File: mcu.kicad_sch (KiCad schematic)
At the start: 5 parts, among them J3 USB_C_Receptacle_USB2.0_16P, M1 Module-stlink-0.1, M3 Module-mega-mcu144-0.6

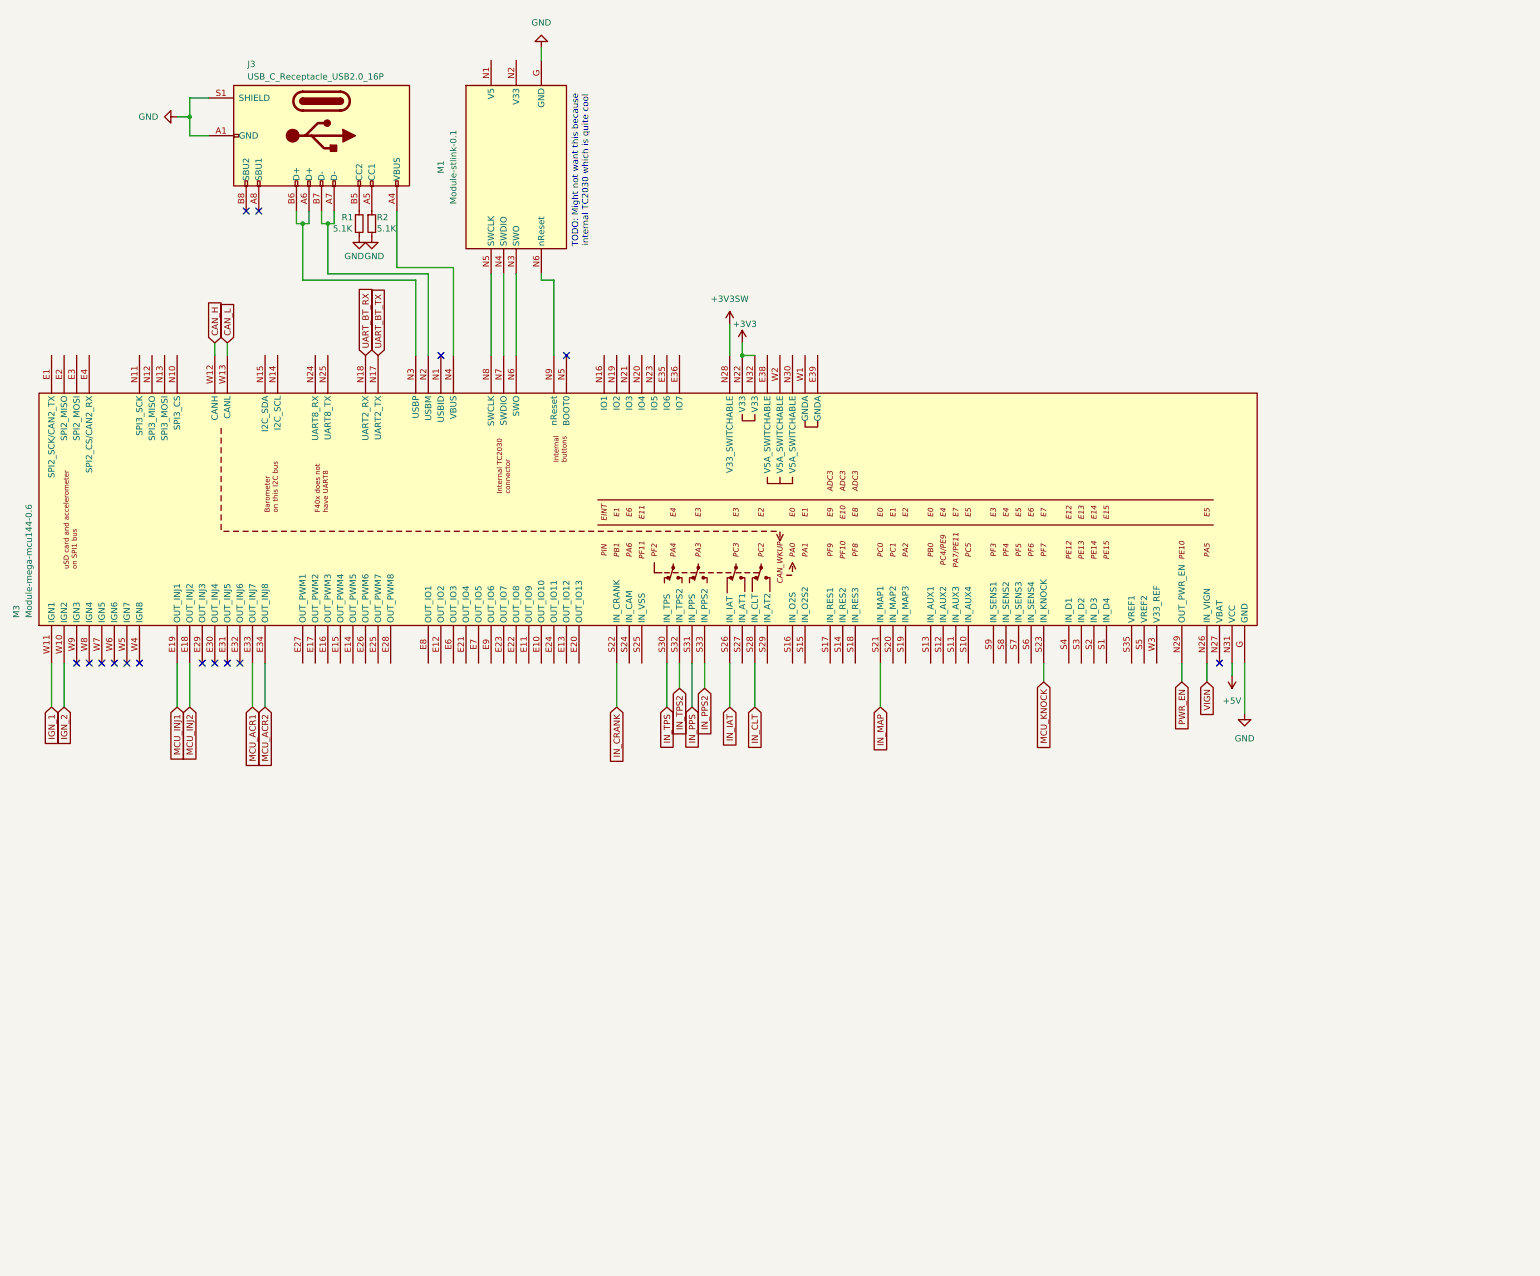
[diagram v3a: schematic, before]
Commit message: igntion igbt, cooling mosfet
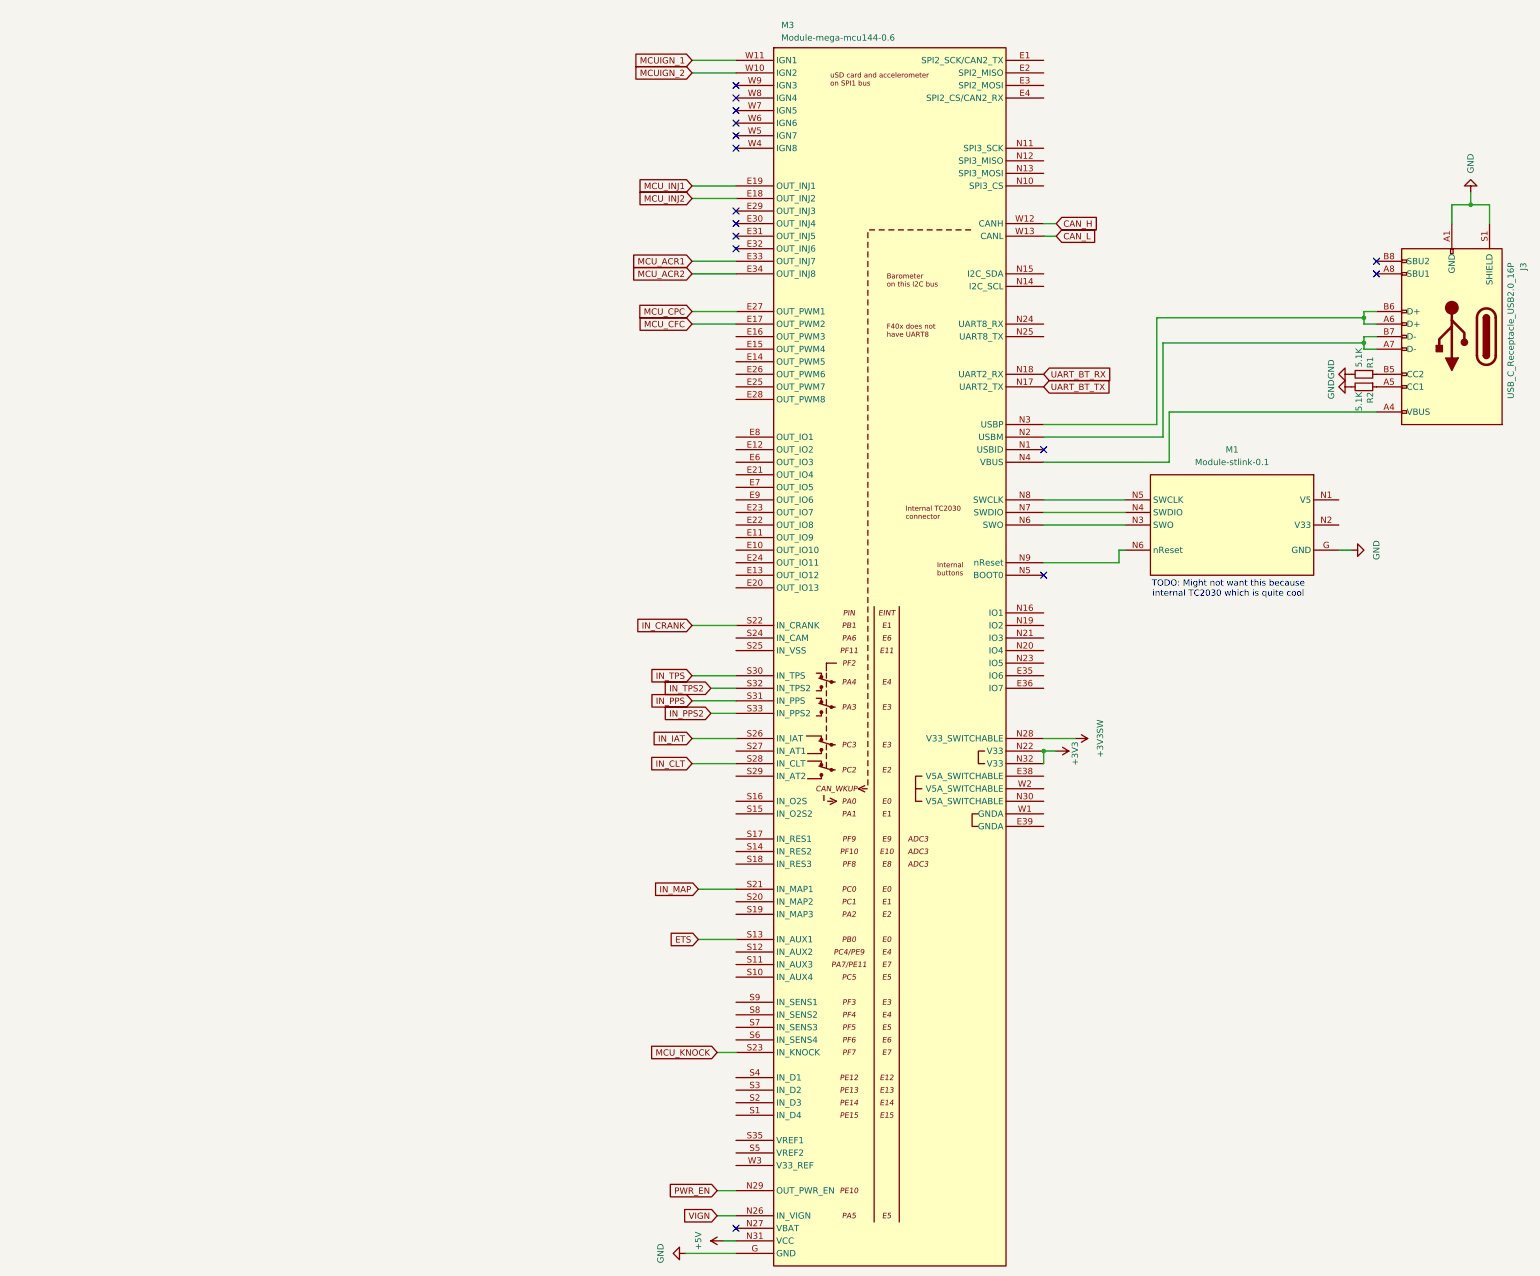
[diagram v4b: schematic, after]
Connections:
- net MCU_CFC: now reaches M3.E17 (OUT_PWM2)
- net MCU_CPC: now reaches M3.E27 (OUT_PWM1)
- net ETS: now reaches M3.S13 (IN_AUX1)
- net IGN_1 renamed MCUIGN_1
- net IGN_2 renamed MCUIGN_2
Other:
- moved on the sheet: J3, M1, M3, R1, R2

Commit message: trying out a layout and routing
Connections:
- net +5VA: now reaches M3.E38 (V5A_SWITCHABLE)
- net +5VA: now also M3.W2 (V5A_SWITCHABLE)
- net H2OSPC: now reaches M3.S11 (IN_AUX3)
- net H2OS2: now reaches M3.S15 (IN_O2S2)
- net H2OS1: now reaches M3.S16 (IN_O2S)
- net IN_JSS: now reaches M3.S17 (IN_RES1)
- net IN_AAT: now reaches M3.S27 (IN_AT1)
- net MCU_KNOCK_R: now reaches M3.S9 (IN_SENS1)
- net GNDA: now reaches M3.W1 (GNDA)
- net MCU_KNOCK renamed MCU_KNOCK_F
- no-connect marks 15 -> 17
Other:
- note added: "TODO: Do we really need post CAT?"

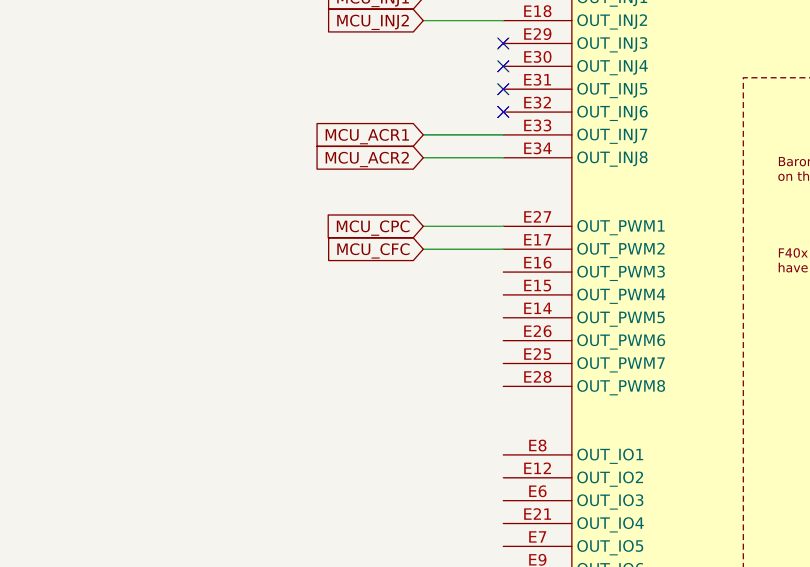
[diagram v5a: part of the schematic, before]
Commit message: adding electronic throttle control
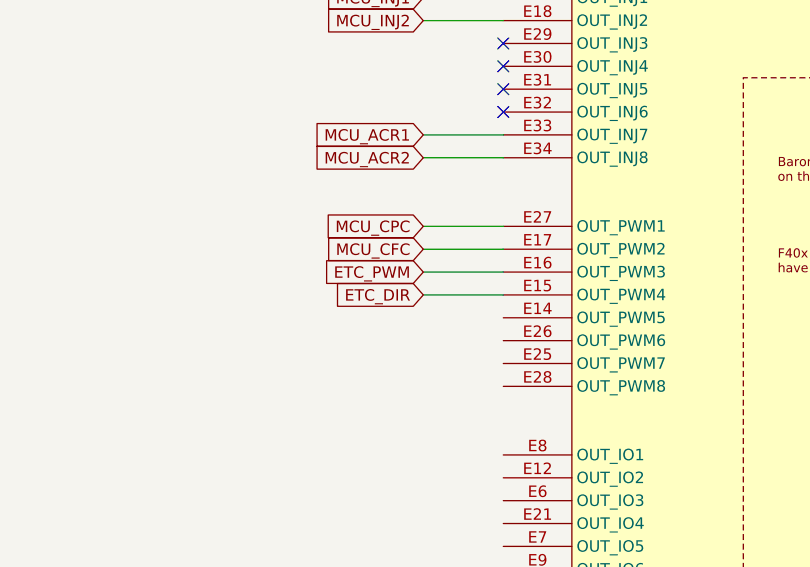
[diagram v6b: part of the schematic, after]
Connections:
- net ETC_DIR: now reaches M3.E15 (OUT_PWM4)
- net ETC_PWM: now reaches M3.E16 (OUT_PWM3)
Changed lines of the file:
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@@
+	(wire
+		(pts
+			(xy 160.02 83.82) (xy 168.91 83.82)
+		)
+		(stroke
+			(width 0)
+			(type default)
+		)
+	)
 	(wire
 		(pts
@@
 		(pts
 			(xy 317.5 52.07) (xy 317.5 54.61)
+		)
+		(stroke
+			(width 0)
+			(type default)
+		)
+	)
+	(wire
+		(pts
+			(xy 160.02 81.28) (xy 168.91 81.28)
 		)
 		(stroke
@@
 		)
 	)
+	(global_label "ETC_DIR"
+		(shape input)
+		(at 160.02 83.82 180)
+		(fields_autoplaced yes)
+		(effects
+			(font
+				(size 1.27 1.27)
+			)
+			(justify right)
+		)
+		(property "Intersheetrefs" "${INTERSHEET_REFS}"
+			(at 149.5358 83.82 0)
+			(effects
+				(font
+					(size 1.27 1.27)
+				)
+				(justify right)
+				(hide yes)
+			)
+		)
+	)
 	(global_label "IN_CLT"
 		(shape input)
@@
 			(effects
 				(font
+					(size 1.27 1.27)
+				)
+				(justify right)
+				(hide yes)
+			)
+		)
+	)
+	(global_label "ETC_PWM"
+		(shape input)
+		(at 160.02 81.28 180)
+		(fields_autoplaced yes)
+		(effects
+			(font
+				(size 1.27 1.27)
+			)
+			(justify right)
+		)
+		(property "Intersheetrefs" "${INTERSHEET_REFS}"
+			(at 148.5078 81.28 0)
+			(effects
+				(font
